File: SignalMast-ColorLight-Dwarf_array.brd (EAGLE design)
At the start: 108.6 x 103.5 mm, 49 parts

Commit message: added missing values
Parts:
- BOARD1: value (none) -> 10x10
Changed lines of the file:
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@@
 </autorouter>
 <elements>
-<element name="BOARD1" library="SPCoast" package="BOARD-SEEED10X10-NOHOLES" value="" x="0" y="0"/>
+<element name="BOARD1" library="SPCoast" package="BOARD-SEEED10X10-NOHOLES" value="10x10" x="0" y="0"/>
 <element name="GYR+" library="SPCoast" package="1X04_LOCK" value="CONNECTOR-GROVE-4P-2.0-3470130P1" x="22.86" y="3.81" smashed="yes" rot="R180"/>
 <element name="LED1" library="SPCoast" package="0603-LED" value="R" x="19.05" y="16.51" smashed="yes" rot="R180">

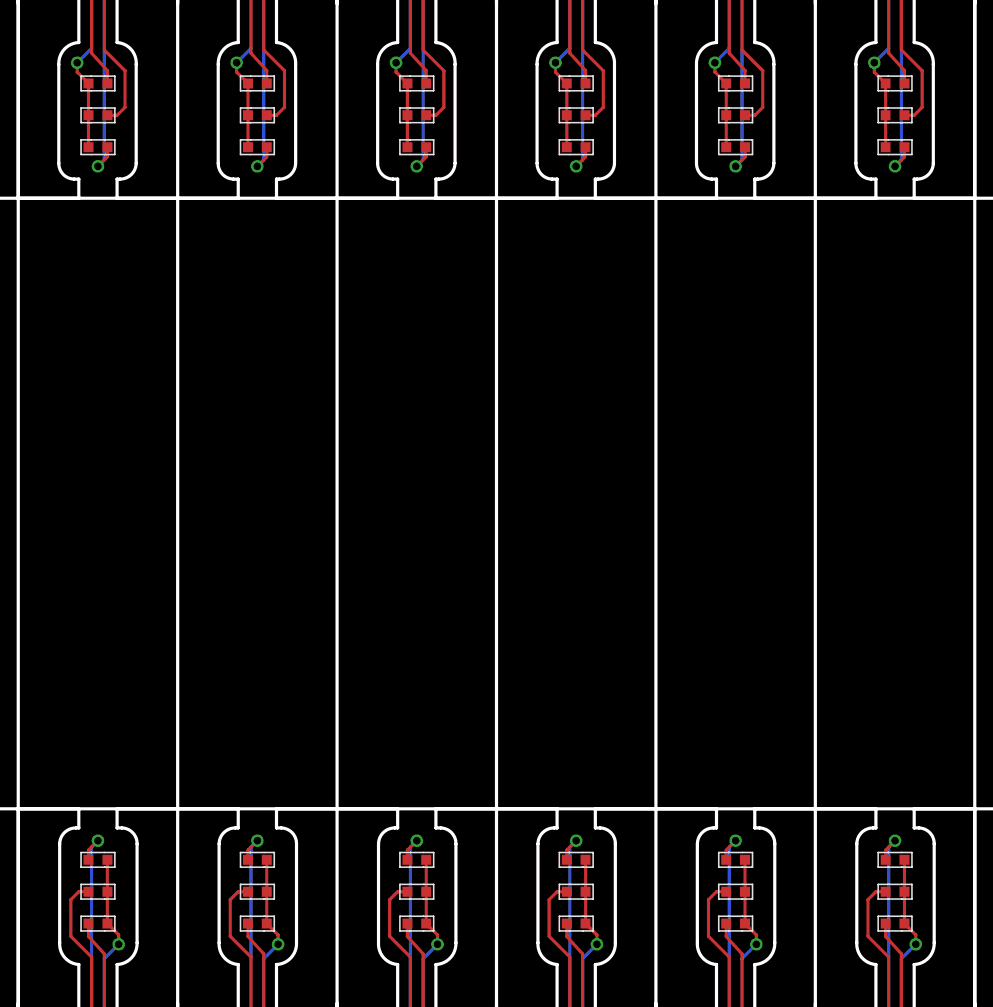
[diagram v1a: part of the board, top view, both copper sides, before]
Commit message: normalized values
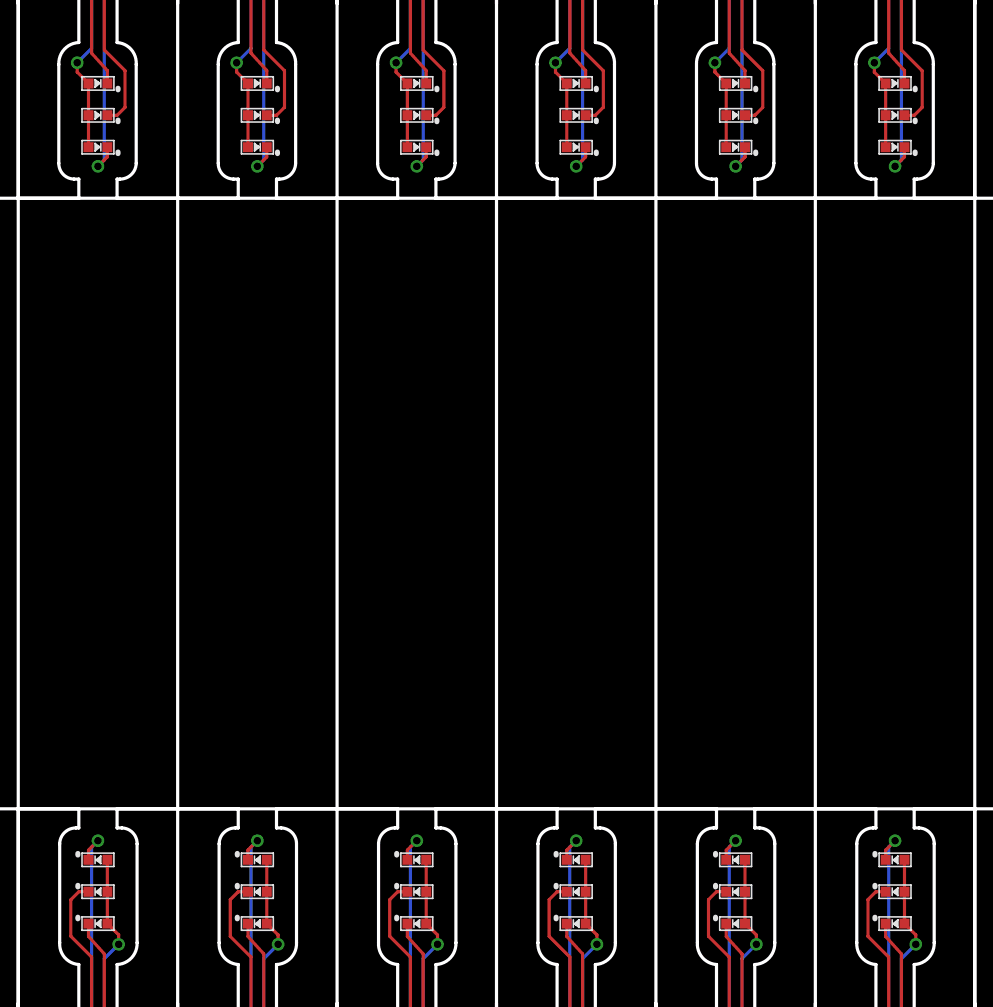
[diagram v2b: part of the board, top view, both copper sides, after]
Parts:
- BOARD1: value 10x10 -> BOARD
- GYR+, GYR+1, GYR+10, GYR+11, GYR+2, GYR+3, GYR+4, GYR+5, GYR+6, GYR+7, GYR+8, GYR+9: value CONNECTOR-GROVE-4P-2.0-3470130P1 -> 0.100
- turned LED1 to 0 degrees
- turned LED10 to 0 degrees
- turned LED11 to 0 degrees
- turned LED12 to 0 degrees
- turned LED13 to 0 degrees
- turned LED14 to 0 degrees
- turned LED15 to 0 degrees
- turned LED16 to 0 degrees
- turned LED17 to 0 degrees
- turned LED18 to 0 degrees
- turned LED19 to 180 degrees
- turned LED2 to 0 degrees
- turned LED20 to 180 degrees
- turned LED21 to 180 degrees
- turned LED22 to 180 degrees
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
